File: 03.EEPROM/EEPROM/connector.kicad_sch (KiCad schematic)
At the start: 4 parts, among them J1 Conn_01x04_Pin, J2 Conn_01x04_Pin, J3 Conn_01x09_Pin, J4 Conn_02x03_Odd_Even

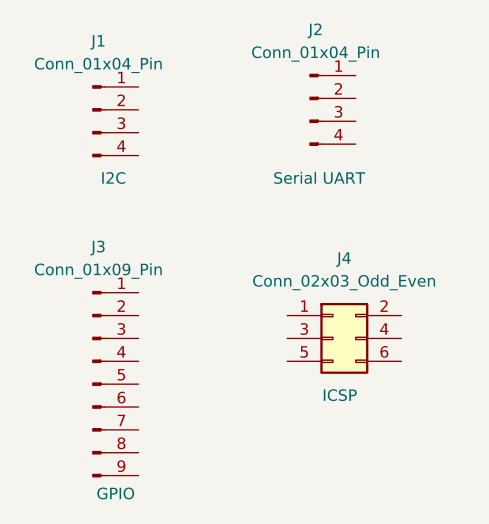
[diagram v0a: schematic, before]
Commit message: EEPROM - EESCHEMA - ARRANGE, ANNOTATE
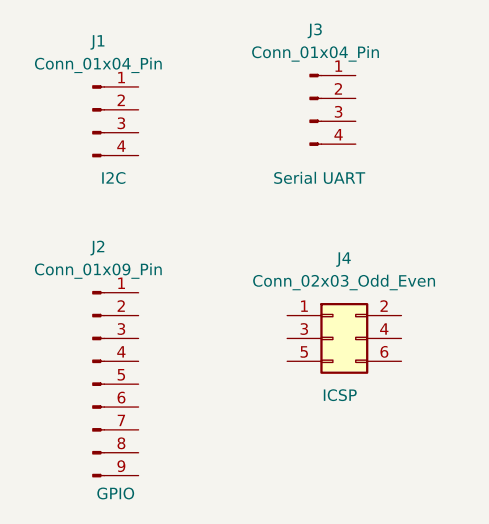
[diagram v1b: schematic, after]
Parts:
- renumbered J3 to J2, J2 to J3
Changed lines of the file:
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@@
 		(on_board yes)
 		(dnp no)
-		(property "Reference" "J2"
+		(property "Reference" "J3"
 			(at 100.965 62.23 0)
 			(effects
@@
 			(project "EEPROM"
 				(path "/b4f5f33e-7286-44f8-9677-0db3208b5bbd/d76e24af-64fe-4fa3-a6dd-5371cafe37dc"
-					(reference "J2")
+					(reference "J3")
 					(unit 1)
 				)
@@
 		(on_board yes)
 		(dnp no)
-		(property "Reference" "J3"
+		(property "Reference" "J2"
 			(at 76.835 86.36 0)
 			(effects
@@
 			(project ""
 				(path "/b4f5f33e-7286-44f8-9677-0db3208b5bbd/d76e24af-64fe-4fa3-a6dd-5371cafe37dc"
-					(reference "J3")
+					(reference "J2")
 					(unit 1)
 				)

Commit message: EEPROM - EESCHEMA - ASSOCIATE
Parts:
- J1, J3: footprint (none) -> Connector_PinHeader_2.54mm:PinHeader_1x04_P2.54mm_Vertical
- J2: footprint (none) -> Connector_PinHeader_2.54mm:PinHeader_1x09_P2.54mm_Vertical
- J4: footprint (none) -> Connector_PinHeader_2.54mm:PinHeader_2x03_P2.54mm_Vertical
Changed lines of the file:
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@@
 			)
 		)
-		(property "Footprint" ""
+		(property "Footprint" "Connector_PinHeader_2.54mm:PinHeader_1x04_P2.54mm_Vertical"
 			(at 100.33 69.85 0)
 			(effects
@@
 			)
 		)
-		(property "Footprint" ""
+		(property "Footprint" "Connector_PinHeader_2.54mm:PinHeader_2x03_P2.54mm_Vertical"
 			(at 102.87 96.52 0)
 			(effects
@@
 			)
 		)
-		(property "Footprint" ""
+		(property "Footprint" "Connector_PinHeader_2.54mm:PinHeader_1x04_P2.54mm_Vertical"
 			(at 76.2 71.12 0)
 			(effects
@@
 			)
 		)
-		(property "Footprint" ""
+		(property "Footprint" "Connector_PinHeader_2.54mm:PinHeader_1x09_P2.54mm_Vertical"
 			(at 76.2 101.6 0)
 			(effects

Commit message: EEPROM - EESCHEMA - WIRING 2
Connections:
- net GND: now reaches J3.1 (Pin_1)
- net GND: now also J1.1 (Pin_1), J2.8 (Pin_8), J4.6 (Pin_6)
- net Vcc: now reaches J3.2 (Pin_2)
- net Vcc: now also J1.2 (Pin_2), J2.9 (Pin_9), J4.2 (Pin_2)
- net RX: now reaches J3.3 (Pin_3)
- net TX: now reaches J3.4 (Pin_4)
- net MISO: now reaches J4.1 (Pin_1)
- net SCK: now reaches J4.3 (Pin_3)
- net SCK: now also J1.4 (Pin_4)
- net MOSI: now reaches J4.4 (Pin_4)
- net RESET: now reaches J4.5 (Pin_5)
- net SDA: now reaches J1.3 (Pin_3)
- net D2: now reaches J2.1 (Pin_1)
- net D3: now reaches J2.2 (Pin_2)
- net D4: now reaches J2.3 (Pin_3)
- net D5: now reaches J2.4 (Pin_4)
- net D6: now reaches J2.5 (Pin_5)
- net D7: now reaches J2.6 (Pin_6)
- net D8: now reaches J2.7 (Pin_7)
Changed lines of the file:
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@@
 	(generator_version "9.0")
 	(paper "A4")
+	(hierarchical_label "D8"
+		(shape bidirectional)
+		(at 81.28 106.68 0)
+		(effects
+			(font
+				(size 1.27 1.27)
+			)
+			(justify left)
+		)
+	)
+	(hierarchical_label "D2"
+		(shape bidirectional)
+		(at 81.28 91.44 0)
+		(effects
+			(font
+				(size 1.27 1.27)
+			)
+			(justify left)
+		)
+	)
+	(hierarchical_label "TX"
+		(shape output)
+		(at 105.41 74.93 0)
+		(effects
+			(font
+				(size 1.27 1.27)
+			)
+			(justify left)
+		)
+	)
+	(hierarchical_label "MOSI"
+		(shape input)
+		(at 110.49 96.52 0)
+		(effects
+			(font
+				(size 1.27 1.27)
+			)
+			(justify left)
+		)
+	)
+	(hierarchical_label "Vcc"
+		(shape passive)
+		(at 110.49 93.98 0)
+		(effects
+			(font
+				(size 1.27 1.27)
+			)
+			(justify left)
+		)
+	)
+	(hierarchical_label "GND"
+		(shape passive)
+		(at 105.41 67.31 0)
+		(effects
+			(font
+				(size 1.27 1.27)
+			)
+			(justify left)
+		)
+	)
+	(hierarchical_label "GND"
+		(shape passive)
+		(at 81.28 68.58 0)
+		(effects
+			(font
+				(size 1.27 1.27)
+			)
+			(justify left)
+		)
+	)
+	(hierarchical_label "D6"
+		(shape bidirectional)
+		(at 81.28 101.6 0)
+		(effects
+			(font
+				(size 1.27 1.27)
+			)
+			(justify left)
+		)
+	)
+	(hierarchical_label "SCK"
+		(shape passive)
+		(at 81.28 76.2 0)
+		(effects
+			(font
+				(size 1.27 1.27)
+			)
+			(justify left)
+		)
+	)
+	(hierarchical_label "SCK"
+		(shape passive)
+		(at 97.79 96.52 180)
+		(effects
+			(font
+				(size 1.27 1.27)
+			)
+			(justify right)
+		)
+	)
+	(hierarchical_label "D7"
+		(shape bidirectional)
+		(at 81.28 104.14 0)
+		(effects
+			(font
+				(size 1.27 1.27)
+			)
+			(justify left)
+		)
+	)
+	(hierarchical_label "D3"
+		(shape bidirectional)
+		(at 81.28 93.98 0)
+		(effects
+			(font
+				(size 1.27 1.27)
+			)
+			(justify left)
+		)
+	)
+	(hierarchical_label "D5"
+		(shape bidirectional)
+		(at 81.28 99.06 0)
+		(effects
+			(font
+				(size 1.27 1.27)
+			)
+			(justify left)
+		)
+	)
+	(hierarchical_label "Vcc"
+		(shape passive)
+		(at 81.28 71.12 0)
+		(effects
+			(font
+				(size 1.27 1.27)
+			)
+			(justify left)
+		)
+	)
+	(hierarchical_label "Vcc"
+		(shape passive)
+		(at 81.28 111.76 0)
+		(effects
+			(font
+				(size 1.27 1.27)
+			)
+			(justify left)
+		)
+	)
+	(hierarchical_label "RX"
+		(shape input)
+		(at 105.41 72.39 0)
+		(effects
+			(font
+				(size 1.27 1.27)
+			)
+			(justify left)
+		)
+	)
+	(hierarchical_label "GND"
+		(shape passive)
+		(at 81.28 109.22 0)
+		(effects
+			(font
+				(size 1.27 1.27)
+			)
+			(justify left)
+		)
+	)
+	(hierarchical_label "D4"
+		(shape bidirectional)
+		(at 81.28 96.52 0)
+		(effects
+			(font
+				(size 1.27 1.27)
+			)
+			(justify left)
+		)
+	)
+	(hierarchical_label "GND"
+		(shape passive)
+		(at 110.49 99.06 0)
+		(effects
+			(font
+				(size 1.27 1.27)
+			)
+			(justify left)
+		)
+	)
+	(hierarchical_label "SDA"
+		(shape bidirectional)
+		(at 81.28 73.66 0)
+		(effects
+			(font
+				(size 1.27 1.27)
+			)
+			(justify left)
+		)
+	)
+	(hierarchical_label "MISO"
+		(shape output)
+		(at 97.79 93.98 180)
+		(effects
+			(font
+				(size 1.27 1.27)
+			)
+			(justify right)
+		)
+	)
+	(hierarchical_label "RESET"
+		(shape passive)
+		(at 97.79 99.06 180)
+		(effects
+			(font
+				(size 1.27 1.27)
+			)
+			(justify right)
+		)
+	)
+	(hierarchical_label "Vcc"
+		(shape passive)
+		(at 105.41 69.85 0)
+		(effects
+			(font
+				(size 1.27 1.27)
+			)
+			(justify left)
+		)
+	)
 	(symbol
 		(lib_id "Connector:Conn_01x04_Pin")
